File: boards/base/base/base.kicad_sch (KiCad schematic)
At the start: 18 parts, among them J1 Conn_01x04_Female, J2 Conn_01x06_Female, J3 Conn_01x06_Female, Q1 BC547, Q2 BC547, Q3 2SD1047, U1 XL1509-5.0, U2 ESP32-S3-DevKitC

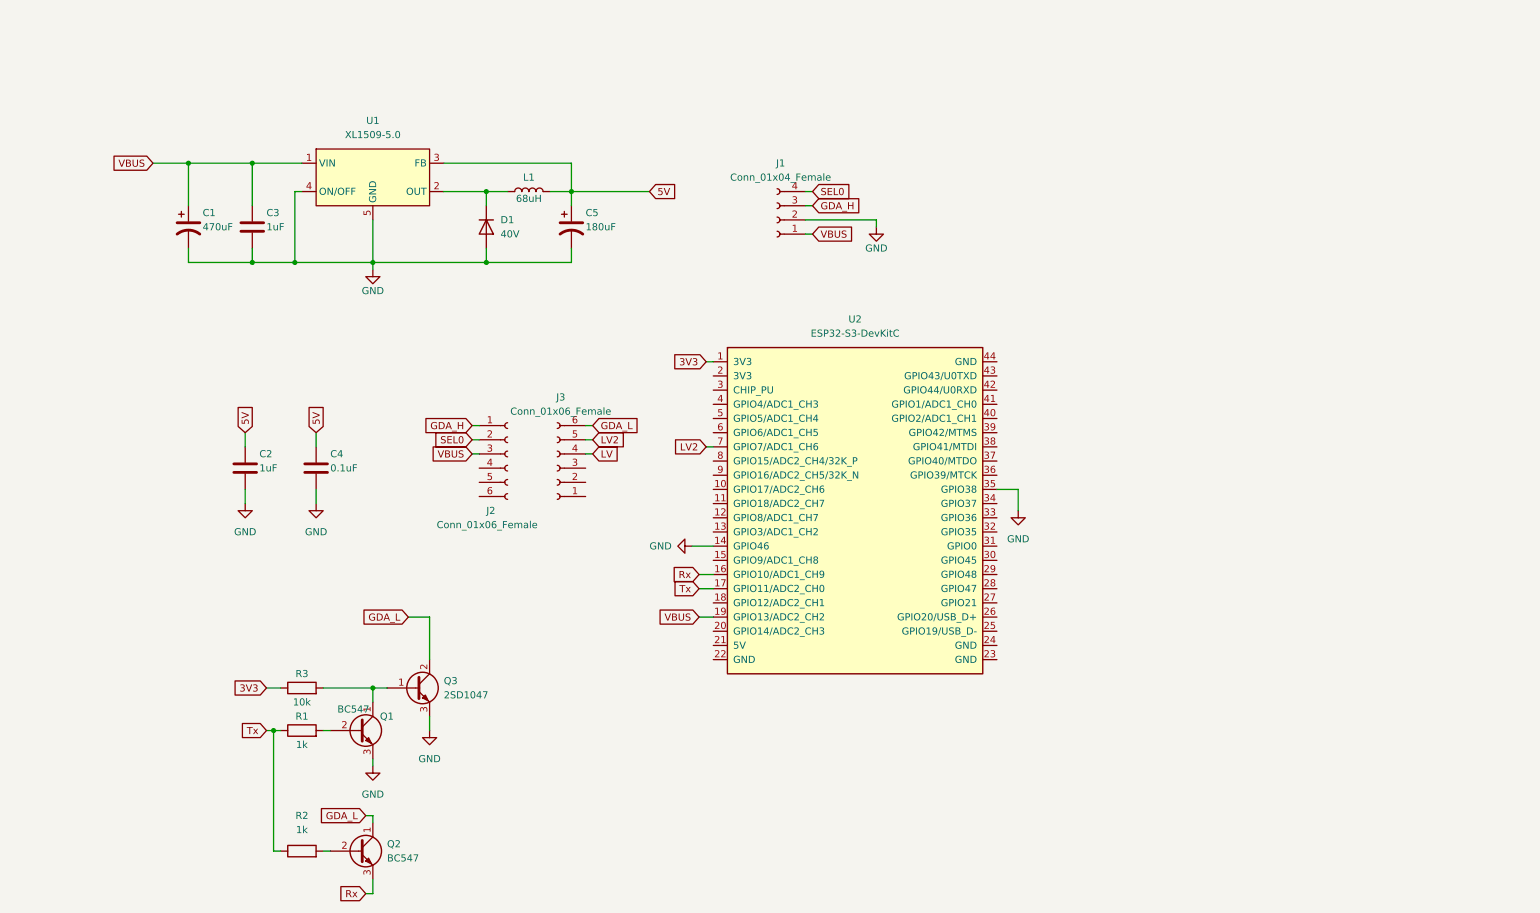
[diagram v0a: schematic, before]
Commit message: Finished BasePCB
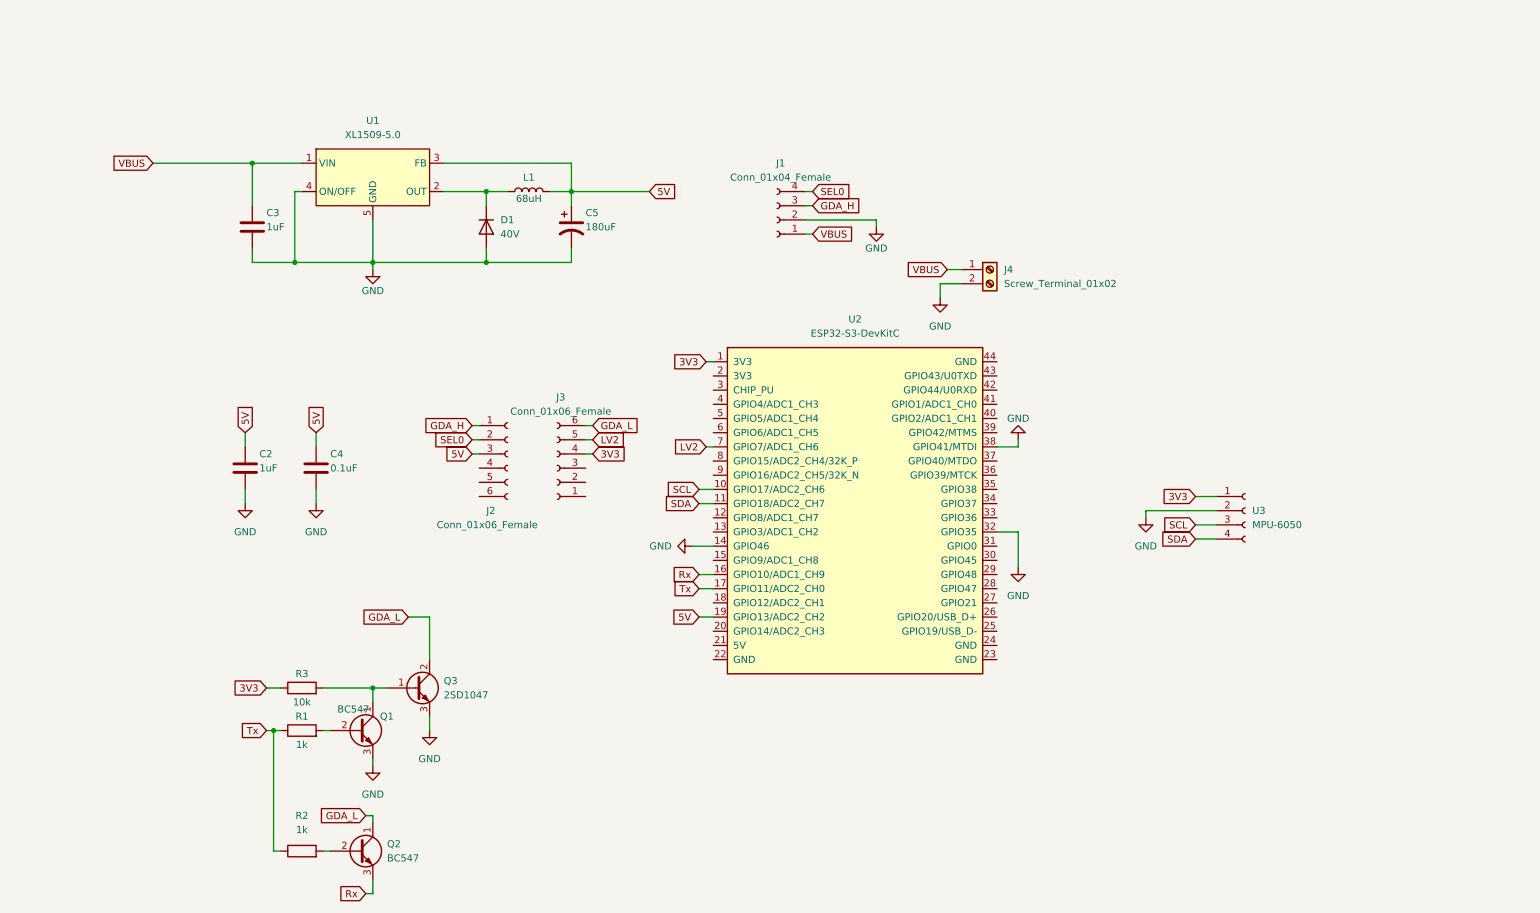
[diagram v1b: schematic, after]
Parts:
- removed C1: 470uF, Capacitor_THT:C_Radial_D12.5mm_H20.0mm_P5.00mm, symbol Device:C_Polarized_US
- added J4: Screw_Terminal_01x02, TerminalBlock_Altech:Altech_AK300_1x02_P5.00mm_45-Degree, symbol Connector:Screw_Terminal_01x02
- added U3: MPU-6050, Connector_PinHeader_2.54mm:PinHeader_1x04_P2.54mm_Vertical, symbol Connector:Conn_01x04_Female
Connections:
- net LV is gone; now on net 3V3: J3.4 (Pin_4)
- net 3V3: now also U3.1 (Pin_1)
- net 5V: now also J2.3 (Pin_3), U2.19 (GPIO13/ADC2_CH2)
- net GND: now also U2.32 (GPIO35), U2.38 (GPIO41/MTDI), J4.2 (Pin_2), U3.2 (Pin_2); no longer U2.35 (GPIO38)
- net VBUS: now also J4.1 (Pin_1); no longer J2.3 (Pin_3), U2.19 (GPIO13/ADC2_CH2)
- net SCL: now reaches U2.10 (GPIO17/ADC2_CH6)
- net SCL: now also U3.3 (Pin_3)
- net SDA: now reaches U2.11 (GPIO18/ADC2_CH7)
- net SDA: now also U3.4 (Pin_4)

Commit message: Added cab_reset and base LED
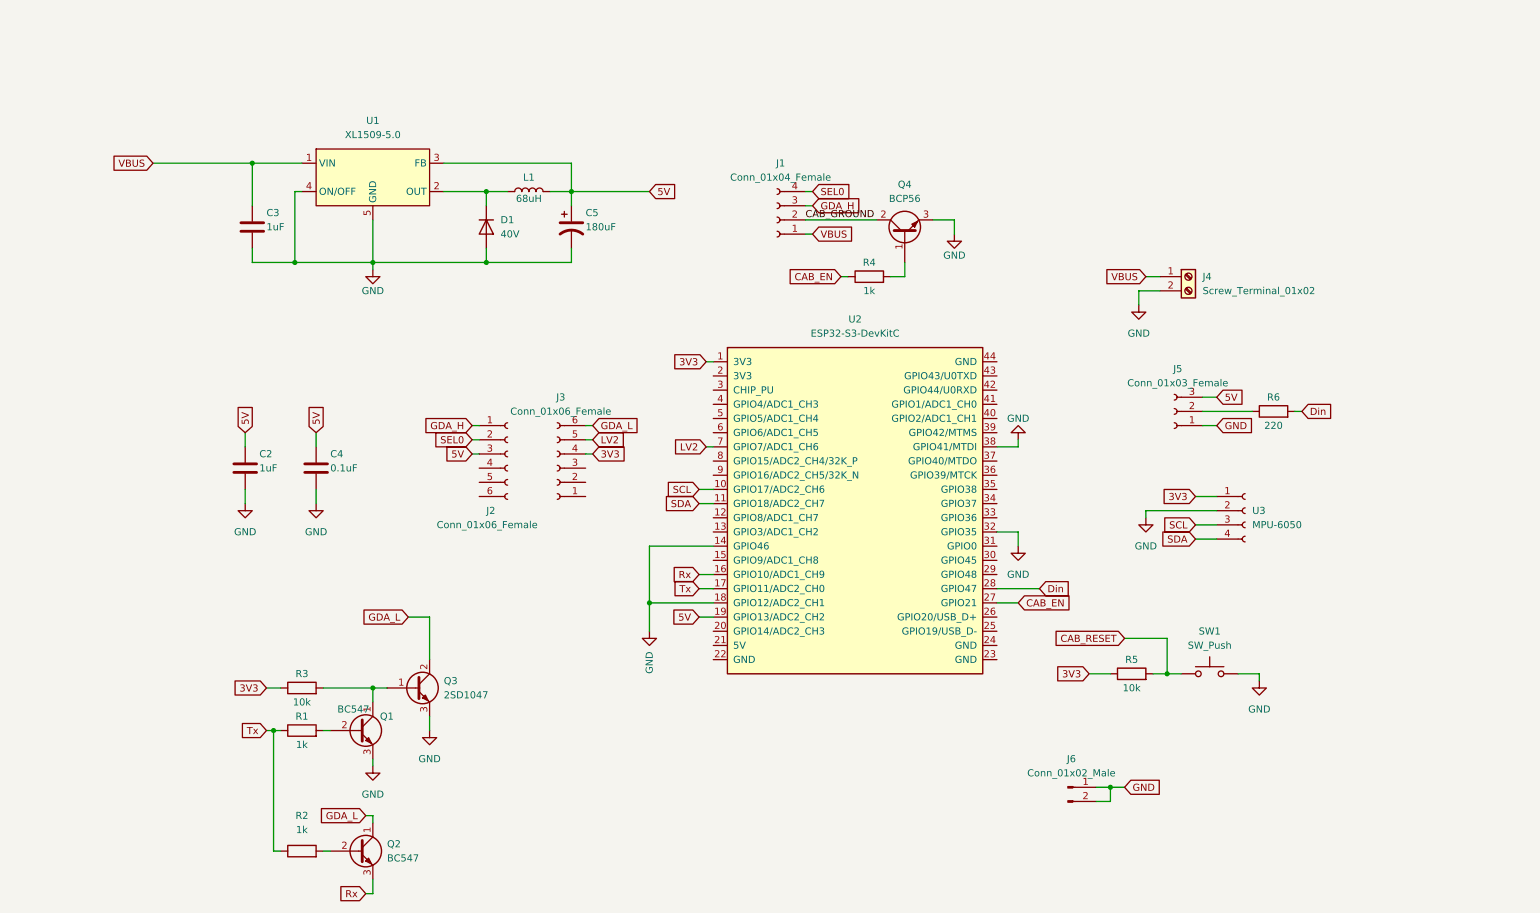
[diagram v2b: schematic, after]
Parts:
- added J5: Conn_01x03_Female, Connector_PinHeader_2.54mm:PinHeader_1x03_P2.54mm_Vertical, symbol Connector:Conn_01x03_Female
- added J6: Conn_01x02_Male, TerminalBlock:TerminalBlock_Altech_AK300-2_P5.00mm, symbol Connector:Conn_01x02_Male
- added Q4: BCP56, Package_TO_SOT_SMD:TO-263-3_TabPin2, symbol Transistor_BJT:BCP56
- added R4: 1k, Resistor_SMD:R_0805_2012Metric, symbol Device:R
- added R5: 10k, Resistor_SMD:R_0805_2012Metric, symbol Device:R
- added R6: 220, Resistor_SMD:R_0805_2012Metric, symbol Device:R
- added SW1: SW_Push, TerminalBlock_4Ucon:TerminalBlock_4Ucon_1x02_P3.50mm_Vertical, symbol Switch:SW_Push
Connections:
- net 3V3: now also R5.1
- net 5V: now also J5.3 (Pin_3)
- net GND: now also U2.18 (GPIO12/ADC2_CH1), J5.1 (Pin_1), J6.1 (Pin_1), J6.2 (Pin_2), Q4.3 (E), SW1.2; no longer J1.2 (Pin_2)
- net CAB_EN: now reaches U2.27 (GPIO21)
- net CAB_EN: now also R4.1
- net Din: now reaches U2.28 (GPIO47)
- net Din: now also R6.2
- new net: J5.2 (Pin_2), R6.1
- new net: Q4.1 (B), R4.2
- new net CAB_GROUND: J1.2 (Pin_2), Q4.2 (C), Q4.4 (C)
- new net CAB_RESET: R5.2, SW1.1
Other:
- moved on the sheet: J4

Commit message: Final version of BasePCB
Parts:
- removed R6: 220, Resistor_SMD:R_0805_2012Metric, symbol Device:R
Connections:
- net CAB_EN: now also U2.29 (GPIO48); no longer U2.27 (GPIO21)
- net Din: now also J5.2 (Pin_2), U2.30 (GPIO45); no longer U2.28 (GPIO47)
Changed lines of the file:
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@@
+    (stroke (width 0) (type default) (color 0 0 0 0))
+  )
+  (wire (pts (xy 189.23 110.49) (xy 191.77 110.49))
     (stroke (width 0) (type default) (color 0 0 0 0))
   )
@@
     (stroke (width 0) (type default) (color 0 0 0 0))
   )
-  (wire (pts (xy 189.23 115.57) (xy 196.85 115.57))
-    (stroke (width 0) (type default) (color 0 0 0 0))
-  )
   (wire (pts (xy 137.16 90.17) (xy 138.43 90.17))
     (stroke (width 0) (type default) (color 0 0 0 0))
   )
-  (wire (pts (xy 189.23 118.11) (xy 193.04 118.11))
-    (stroke (width 0) (type default) (color 0 0 0 0))
-  )
   (wire (pts (xy 95.25 91.44) (xy 96.52 91.44))
     (stroke (width 0) (type default) (color 0 0 0 0))
@@
     (stroke (width 0) (type default) (color 0 0 0 0))
   )
-  (wire (pts (xy 242.57 83.82) (xy 243.84 83.82))
-    (stroke (width 0) (type default) (color 0 0 0 0))
-  )
   (wire (pts (xy 209.55 151.13) (xy 209.55 153.67))
     (stroke (width 0) (type default) (color 0 0 0 0))
@@
     (stroke (width 0) (type default) (color 0 0 0 0))
   )
-  (wire (pts (xy 189.23 105.41) (xy 193.04 105.41))
+  (wire (pts (xy 189.23 105.41) (xy 205.74 105.41))
     (stroke (width 0) (type default) (color 0 0 0 0))
   )
@@
     (stroke (width 0) (type default) (color 0 0 0 0))
   )
-  (wire (pts (xy 193.04 105.41) (xy 193.04 107.95))
-    (stroke (width 0) (type default) (color 0 0 0 0))
-  )
   (wire (pts (xy 232.41 130.81) (xy 236.22 130.81))
     (stroke (width 0) (type default) (color 0 0 0 0))
@@
     (stroke (width 0) (type default) (color 0 0 0 0))
   )
+  (wire (pts (xy 205.74 105.41) (xy 205.74 107.95))
+    (stroke (width 0) (type default) (color 0 0 0 0))
+  )
   (wire (pts (xy 226.06 81.28) (xy 228.6 81.28))
     (stroke (width 0) (type default) (color 0 0 0 0))
@@
     (stroke (width 0) (type default) (color 0 0 0 0))
   )
-  (wire (pts (xy 226.06 83.82) (xy 234.95 83.82))
+  (wire (pts (xy 226.06 83.82) (xy 228.6 83.82))
     (stroke (width 0) (type default) (color 0 0 0 0))
   )
@@
   )
   (wire (pts (xy 77.47 156.21) (xy 77.47 157.48))
+    (stroke (width 0) (type default) (color 0 0 0 0))
+  )
+  (wire (pts (xy 189.23 113.03) (xy 191.77 113.03))
     (stroke (width 0) (type default) (color 0 0 0 0))
   )
@@
     )
   )
-  (global_label "Din" (shape input) (at 196.85 115.57 0) (fields_autoplaced)
-    (effects (font (size 1.27 1.27)) (justify left))
-    (property "Intersheet References" "${INTERSHEET_REFS}" (id 0) (at 202.2869 115.4906 0)
+  (global_label "Din" (shape input) (at 191.77 110.49 0) (fields_autoplaced)
+    (effects (font (size 1.27 1.27)) (justify left))
+    (property "Intersheet References" "${INTERSHEET_REFS}" (id 0) (at 197.2069 110.4106 0)
       (effects (font (size 1.27 1.27)) (justify left) hide)
     )
@@
     )
   )
-  (global_label "Din" (shape input) (at 243.84 83.82 0) (fields_autoplaced)
-    (effects (font (size 1.27 1.27)) (justify left))
-    (property "Intersheet References" "${INTERSHEET_REFS}" (id 0) (at 249.2769 83.7406 0)
+  (global_label "Din" (shape input) (at 228.6 83.82 0) (fields_autoplaced)
+    (effects (font (size 1.27 1.27)) (justify left))
+    (property "Intersheet References" "${INTERSHEET_REFS}" (id 0) (at 234.0369 83.7406 0)
       (effects (font (size 1.27 1.27)) (justify left) hide)
     )
@@
     )
   )
-  (global_label "CAB_EN" (shape input) (at 193.04 118.11 0) (fields_autoplaced)
-    (effects (font (size 1.27 1.27)) (justify left))
-    (property "Intersheet References" "${INTERSHEET_REFS}" (id 0) (at 202.5288 118.0306 0)
+  (global_label "CAB_EN" (shape input) (at 191.77 113.03 0) (fields_autoplaced)
+    (effects (font (size 1.27 1.27)) (justify left))
+    (property "Intersheet References" "${INTERSHEET_REFS}" (id 0) (at 201.2588 112.9506 0)
       (effects (font (size 1.27 1.27)) (justify left) hide)
     )
@@
   (symbol (lib_id "power:GND") (at 127 123.19 0) (unit 1)
     (in_bom yes) (on_board yes)
-    (property "Reference" "#PWR?" (id 0) (at 127 129.54 0)
+    (property "Reference" "#PWR0102" (id 0) (at 127 129.54 0)
       (effects (font (size 1.27 1.27)) hide)
     )
@@
     (pin "2")
   )
-  (symbol (lib_id "Device:R") (at 238.76 83.82 90) (unit 1)
-    (in_bom yes) (on_board yes)
-    (property "Reference" "R6" (id 0) (at 238.76 81.28 90))
-    (property "Value" "220" (id 1) (at 238.76 86.36 90))
-    (property "Footprint" "Resistor_SMD:R_0805_2012Metric" (id 2) (at 238.76 85.598 90)
-      (effects (font (size 1.27 1.27)) hide)
-    )
-    (property "Datasheet" "~" (id 3) (at 238.76 83.82 0)
-      (effects (font (size 1.27 1.27)) hide)
-    )
-    (pin "1")
-    (pin "2")
-  )
   (symbol (lib_id "Connector:Conn_01x04_Female") (at 233.68 101.6 0) (unit 1)
     (in_bom yes) (on_board yes) (fields_autoplaced)
@@
     (pin "1")
   )
-  (symbol (lib_id "power:GND") (at 193.04 107.95 0) (unit 1)
-    (in_bom yes) (on_board yes) (fields_autoplaced)
-    (property "Reference" "#PWR0101" (id 0) (at 193.04 114.3 0)
-      (effects (font (size 1.27 1.27)) hide)
-    )
-    (property "Value" "GND" (id 1) (at 193.04 113.03 0))
-    (property "Footprint" "" (id 2) (at 193.04 107.95 0)
-      (effects (font (size 1.27 1.27)) hide)
-    )
-    (property "Datasheet" "" (id 3) (at 193.04 107.95 0)
+  (symbol (lib_id "power:GND") (at 205.74 107.95 0) (unit 1)
+    (in_bom yes) (on_board yes)
+    (property "Reference" "#PWR0101" (id 0) (at 205.74 114.3 0)
+      (effects (font (size 1.27 1.27)) hide)
+    )
+    (property "Value" "GND" (id 1) (at 205.74 111.76 0))
+    (property "Footprint" "" (id 2) (at 205.74 107.95 0)
+      (effects (font (size 1.27 1.27)) hide)
+    )
+    (property "Datasheet" "" (id 3) (at 205.74 107.95 0)
       (effects (font (size 1.27 1.27)) hide)
     )
@@
       (reference "#PWR0101") (unit 1) (value "GND") (footprint "")
     )
+    (path "/3528b26f-4b70-42f4-8a61-18d40154b947"
+      (reference "#PWR0102") (unit 1) (value "GND") (footprint "")
+    )
     (path "/e620ee6b-5aa6-4979-b973-5b64ce39d7ba"
       (reference "#PWR0103") (unit 1) (value "GND") (footprint "")
@@
       (reference "#PWR0105") (unit 1) (value "GND") (footprint "")
     )
-    (path "/3528b26f-4b70-42f4-8a61-18d40154b947"
-      (reference "#PWR?") (unit 1) (value "GND") (footprint "")
-    )
     (path "/73408e9c-10be-4e10-ba76-b1dd1086b0ce"
       (reference "C2") (unit 1) (value "1uF") (footprint "Capacitor_SMD:C_0805_2012Metric")
@@
       (reference "R5") (unit 1) (value "10k") (footprint "Resistor_SMD:R_0805_2012Metric")
     )
-    (path "/96e0d4a9-8b7a-4f91-a2ea-64a612b439bb"
-      (reference "R6") (unit 1) (value "220") (footprint "Resistor_SMD:R_0805_2012Metric")
-    )
     (path "/432b8744-344b-4b83-b016-4a2f511d6c04"
